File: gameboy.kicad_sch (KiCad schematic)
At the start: 0 parts

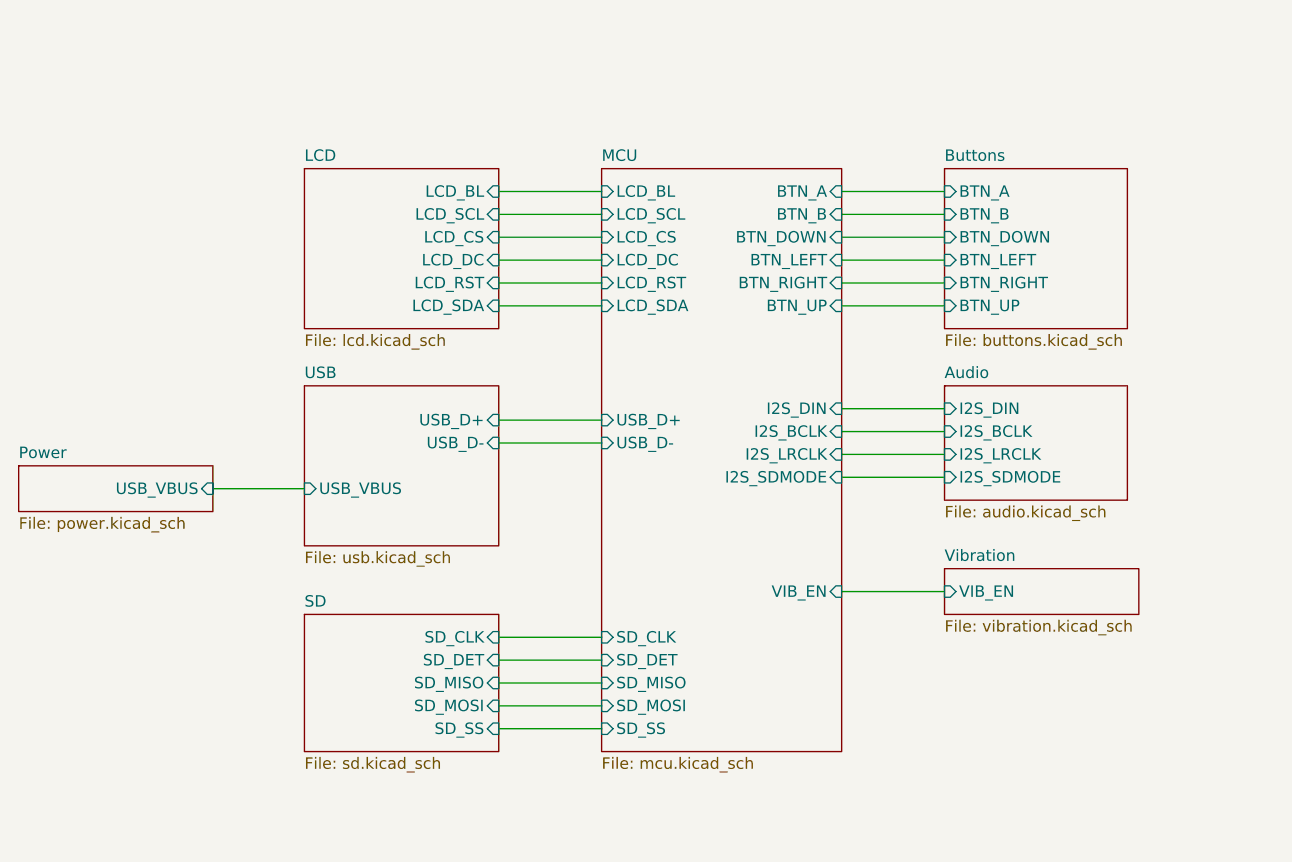
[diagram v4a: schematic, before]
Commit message: add power monitoring
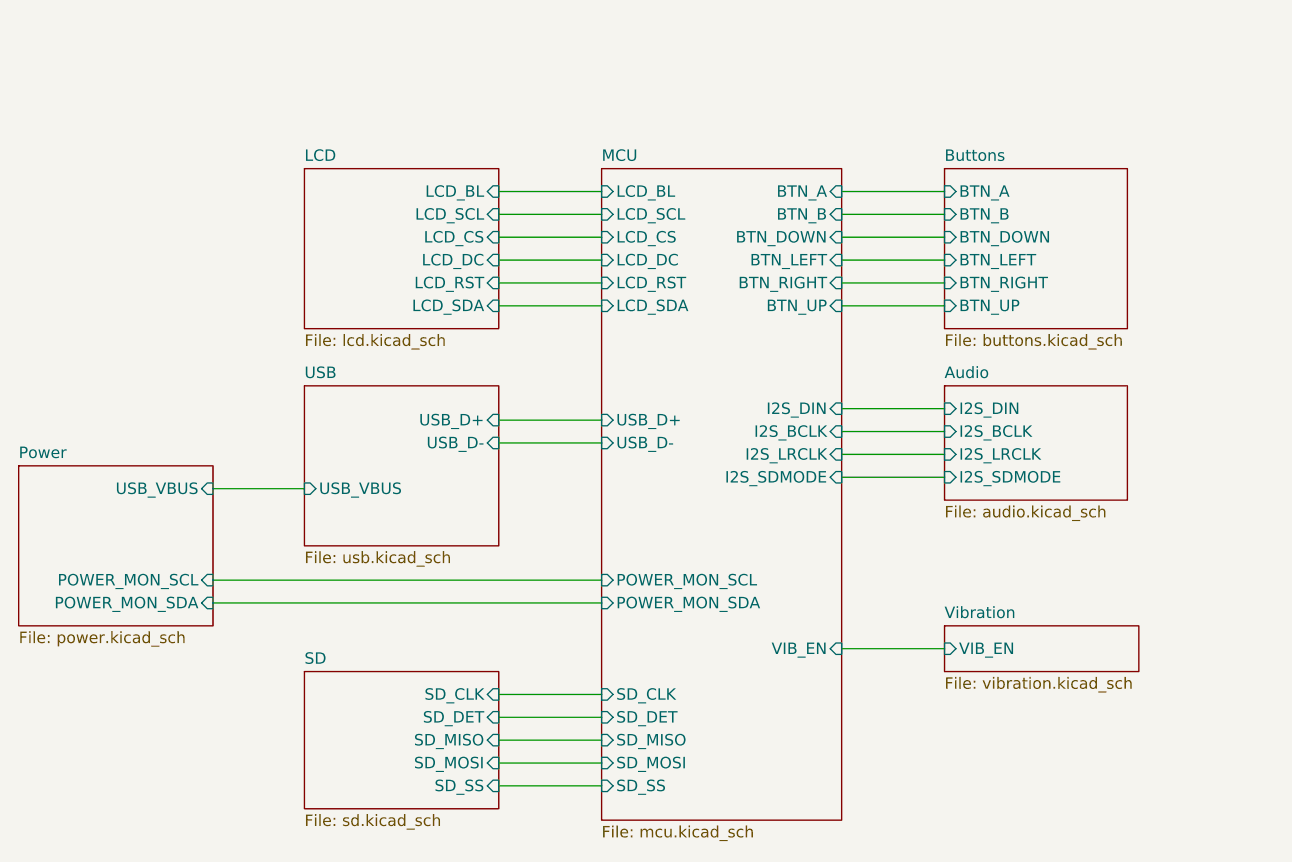
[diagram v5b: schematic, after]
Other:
- sheet MCU ports: added POWER_MON_SCL, POWER_MON_SDA; removed none
- sheet Power ports: added POWER_MON_SCL, POWER_MON_SDA; removed none
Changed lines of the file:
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@@
 	(wire
 		(pts
-			(xy 170.18 119.38) (xy 158.75 119.38)
+			(xy 170.18 125.73) (xy 158.75 125.73)
 		)
 		(stroke
@@
 	(wire
 		(pts
-			(xy 120.65 134.62) (xy 132.08 134.62)
+			(xy 120.65 140.97) (xy 132.08 140.97)
 		)
 		(stroke
@@
 	(wire
 		(pts
-			(xy 120.65 127) (xy 132.08 127)
+			(xy 120.65 133.35) (xy 132.08 133.35)
 		)
 		(stroke
@@
 	(wire
 		(pts
-			(xy 120.65 124.46) (xy 132.08 124.46)
+			(xy 120.65 130.81) (xy 132.08 130.81)
+		)
+		(stroke
+			(width 0)
+			(type default)
+		)
+	)
+	(wire
+		(pts
+			(xy 88.9 118.11) (xy 132.08 118.11)
 		)
 		(stroke
@@
 	(wire
 		(pts
-			(xy 120.65 132.08) (xy 132.08 132.08)
-		)
-		(stroke
-			(width 0)
-			(type default)
-		)
-	)
-	(wire
-		(pts
-			(xy 120.65 129.54) (xy 132.08 129.54)
+			(xy 120.65 138.43) (xy 132.08 138.43)
+		)
+		(stroke
+			(width 0)
+			(type default)
+		)
+	)
+	(wire
+		(pts
+			(xy 120.65 135.89) (xy 132.08 135.89)
+		)
+		(stroke
+			(width 0)
+			(type default)
+		)
+	)
+	(wire
+		(pts
+			(xy 88.9 120.65) (xy 132.08 120.65)
 		)
 		(stroke
@@
 	(sheet
 		(at 132.08 72.39)
-		(size 26.67 64.77)
+		(size 26.67 72.39)
 		(exclude_from_sim no)
 		(in_bom yes)
@@
 		)
 		(property "Sheetfile" "mcu.kicad_sch"
-			(at 132.08 137.7446 0)
+			(at 132.08 145.3646 0)
 			(effects
 				(font
@@
 		)
 		(pin "VIB_EN" input
-			(at 158.75 119.38 0)
+			(at 158.75 125.73 0)
 			(effects
 				(font
@@
 		)
 		(pin "SD_DET" input
-			(at 132.08 127 180)
+			(at 132.08 133.35 180)
 			(effects
 				(font
@@
 		)
 		(pin "SD_MISO" input
-			(at 132.08 129.54 180)
+			(at 132.08 135.89 180)
 			(effects
 				(font
@@
 		)
 		(pin "SD_MOSI" input
-			(at 132.08 132.08 180)
+			(at 132.08 138.43 180)
 			(effects
 				(font
@@
 		)
 		(pin "SD_SS" input
-			(at 132.08 134.62 180)
+			(at 132.08 140.97 180)
 			(effects
 				(font
@@
 		)
 		(pin "SD_CLK" input
-			(at 132.08 124.46 180)
+			(at 132.08 130.81 180)
+			(effects
+				(font
+					(size 1.27 1.27)
+				)
+				(justify left)
+			)
+		)
+		(pin "POWER_MON_SCL" input
+			(at 132.08 118.11 180)
+			(effects
+				(font
+					(size 1.27 1.27)
+				)
+				(justify left)
+			)
+		)
+		(pin "POWER_MON_SDA" input
+			(at 132.08 120.65 180)
 			(effects
 				(font
@@
 	(sheet
 		(at 67.31 105.41)
-		(size 21.59 5.08)
+		(size 21.59 17.78)
 		(exclude_from_sim no)
 		(in_bom yes)
@@
 		)
 		(property "Sheetfile" "power.kicad_sch"
-			(at 67.31 111.0746 0)
+			(at 67.31 123.7746 0)
 			(effects
 				(font
@@
 		(pin "USB_VBUS" input
 			(at 88.9 107.95 0)
+			(effects
+				(font
+					(size 1.27 1.27)
+				)
+				(justify right)
+			)
+		)
+		(pin "POWER_MON_SCL" input
+			(at 88.9 118.11 0)
+			(effects
+				(font
+					(size 1.27 1.27)
+				)
+				(justify right)
+			)
+		)
+		(pin "POWER_MON_SDA" input
+			(at 88.9 120.65 0)
 			(effects
 				(font
@@
 	)
 	(sheet
-		(at 99.06 121.92)
+		(at 99.06 128.27)
 		(size 21.59 15.24)
 		(exclude_from_sim no)
@@
 		)
 		(property "Sheetname" "SD"
-			(at 99.06 121.2084 0)
+			(at 99.06 127.5584 0)
 			(effects
 				(font
@@
 		)
 		(property "Sheetfile" "sd.kicad_sch"
-			(at 99.06 137.7446 0)
+			(at 99.06 144.0946 0)
 			(effects
 				(font
@@
 		)
 		(pin "SD_CLK" input
-			(at 120.65 124.46 0)
+			(at 120.65 130.81 0)
 			(effects
 				(font
@@
 		)
 		(pin "SD_DET" input
-			(at 120.65 127 0)
+			(at 120.65 133.35 0)
 			(effects
 				(font
@@
 		)
 		(pin "SD_MISO" input
-			(at 120.65 129.54 0)
+			(at 120.65 135.89 0)
 			(effects
 				(font
@@
 		)
 		(pin "SD_MOSI" input
-			(at 120.65 132.08 0)
+			(at 120.65 138.43 0)
 			(effects
 				(font
@@
 		)
 		(pin "SD_SS" input
-			(at 120.65 134.62 0)
+			(at 120.65 140.97 0)
 			(effects
 				(font
@@
 	)
 	(sheet
-		(at 170.18 116.84)
+		(at 170.18 123.19)
 		(size 21.59 5.08)
 		(exclude_from_sim no)
@@
 		)
 		(property "Sheetname" "Vibration"
-			(at 170.18 116.1284 0)
+			(at 170.18 122.4784 0)
 			(effects
 				(font
@@
 		)
 		(property "Sheetfile" "vibration.kicad_sch"
-			(at 170.18 122.5046 0)
+			(at 170.18 128.8546 0)
 			(effects
 				(font
@@
 		)
 		(pin "VIB_EN" input
-			(at 170.18 119.38 180)
-			(effects
-				(font
+			(at 170.18 125.73 180)
+			(effects
+				(font
